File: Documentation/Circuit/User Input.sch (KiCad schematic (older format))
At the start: 1 part

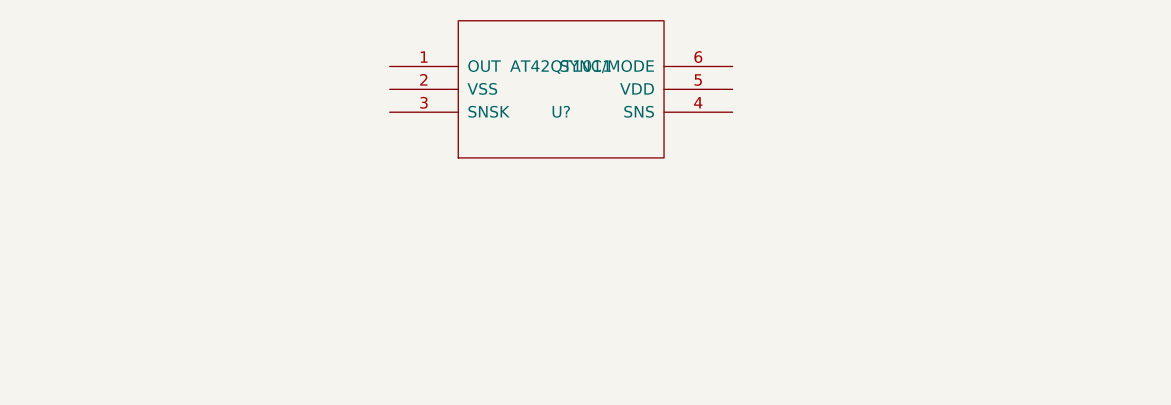
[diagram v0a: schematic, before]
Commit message: Worked on schematic and PCB
Worked on circuit schematic.  Circuits utilized should reflect those in
the BLE112 and AT42 datasheets.  Added initial PCB layout.  Routing
still needs to be done for PCB layout.  Circuit layout should be double
checked before routing.  Refer to an-kd02_103 for more details on touch
interface layout.  Refer to tps62732 datasheet for more details on power
system layout.
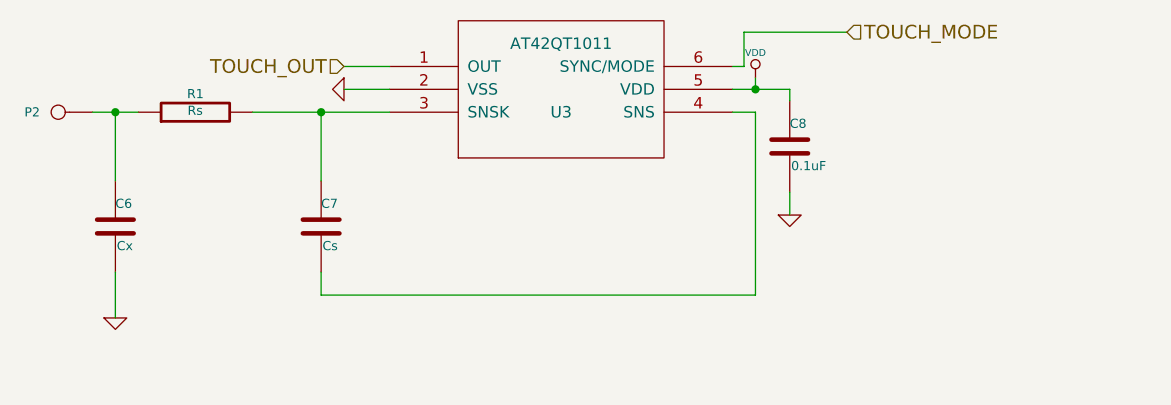
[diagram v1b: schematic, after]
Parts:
- added C6: Cx, ~, symbol C
- added C7: Cs, ~, symbol C
- added C8: 0.1uF, ~, symbol C
- added P2: CONN_1, symbol CONN_1
- added R1: Rs, ~, symbol R
- gave numbers to parts that had none: 1
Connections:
- net TOUCH_OUT: now reaches U3.1 (OUT)
- net GND: now reaches U3.2 (VSS)
- net GND: now also C6.2, C8.2
- net at U3.3 (SNSK): now also C7.1, R1.2
- net at U3.4 (SNS): now also C7.2
- net VDD: now reaches U3.5 (VDD)
- net VDD: now also C8.1
- net TOUCH_MODE: now reaches U3.6 (SYNC/MODE)
- new net: C6.1, P2.1, R1.1
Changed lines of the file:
@@
 Sheet 3 3
 Title ""
-Date "2 jun 2015"
+Date "4 jun 2015"
 Rev ""
 Comp ""
@@
 $EndDescr
 $Comp
-L AT42QT1011 U?
+L AT42QT1011 U3
 U 1 1 556D309E
 P 5450 3600
-F 0 "U?" H 5450 3500 50  0000 C CNN
-F 1 "AT42QT1011" H 5450 3700 50  0000 C CNN
+F 0 "U3" H 5450 3500 50  0000 C CNN
+F 1 "AT42QT1011" H 5450 3800 50  0000 C CNN
 F 2 "MODULE" H 5450 3600 50  0001 C CNN
 F 3 "DOCUMENTATION" H 5450 3600 50  0001 C CNN
@@
 	1    0    0    -1
 $EndComp
+$Comp
+L R R1
+U 1 1 556F5E65
+P 3850 3700
+F 0 "R1" V 3930 3700 40  0000 C CNN
+F 1 "Rs" V 3857 3701 40  0000 C CNN
+F 2 "~" V 3780 3700 30  0000 C CNN
+F 3 "~" H 3850 3700 30  0000 C CNN
+	1    3850 3700
+	0    -1   -1   0
+$EndComp
+$Comp
+L C C7
+U 1 1 556F5E74
+P 4400 4200
+F 0 "C7" H 4400 4300 40  0000 L CNN
+F 1 "Cs" H 4406 4115 40  0000 L CNN
+F 2 "~" H 4438 4050 30  0000 C CNN
+F 3 "~" H 4400 4200 60  0000 C CNN
+	1    4400 4200
+	1    0    0    -1
+$EndComp
+$Comp
+L GND #PWR22
+U 1 1 556F5E91
+P 4500 3600
+F 0 "#PWR22" H 4500 3600 30  0001 C CNN
+F 1 "GND" H 4500 3530 30  0001 C CNN
+F 2 "" H 4500 3600 60  0000 C CNN
+F 3 "" H 4500 3600 60  0000 C CNN
+	1    4500 3600
+	0    1    1    0
+$EndComp
+Wire Wire Line
+	4700 3600 4500 3600
+Wire Wire Line
+	4700 3700 4100 3700
+Wire Wire Line
+	4400 3700 4400 4000
+Connection ~ 4400 3700
+Wire Wire Line
+	4400 4400 4400 4500
+Wire Wire Line
+	6300 3700 6300 4500
+Wire Wire Line
+	6300 3700 6200 3700
+Wire Wire Line
+	6300 4500 4400 4500
+Text HLabel 4500 3500 0    60   Input ~ 0
+TOUCH_OUT
+Wire Wire Line
+	4700 3500 4500 3500
+$Comp
+L VDD #PWR23
+U 1 1 556F5F2B
+P 6300 3550
+F 0 "#PWR23" H 6300 3650 30  0001 C CNN
+F 1 "VDD" H 6300 3660 30  0000 C CNN
+F 2 "" H 6300 3550 60  0000 C CNN
+F 3 "" H 6300 3550 60  0000 C CNN
+	1    6300 3550
+	1    0    0    -1
+$EndComp
+Wire Wire Line
+	6200 3600 6450 3600
+Wire Wire Line
+	6300 3600 6300 3550
+$Comp
+L CONN_1 P2
+U 1 1 556F60DB
+P 3250 3700
+F 0 "P2" H 3330 3700 40  0000 L CNN
+F 1 "CONN_1" H 3250 3755 30  0001 C CNN
+F 2 "" H 3250 3700 60  0000 C CNN
+F 3 "" H 3250 3700 60  0000 C CNN
+	1    3250 3700
+	-1   0    0    1
+$EndComp
+Wire Wire Line
+	3600 3700 3400 3700
+Wire Wire Line
+	3500 3700 3500 4000
+Connection ~ 3500 3700
+$Comp
+L C C6
+U 1 1 556F6108
+P 3500 4200
+F 0 "C6" H 3500 4300 40  0000 L CNN
+F 1 "Cx" H 3506 4115 40  0000 L CNN
+F 2 "~" H 3538 4050 30  0000 C CNN
+F 3 "~" H 3500 4200 60  0000 C CNN
+	1    3500 4200
+	1    0    0    -1
+$EndComp
+$Comp
+L GND #PWR21
+U 1 1 556F6117
+P 3500 4600
+F 0 "#PWR21" H 3500 4600 30  0001 C CNN
+F 1 "GND" H 3500 4530 30  0001 C CNN
+F 2 "" H 3500 4600 60  0000 C CNN
+F 3 "" H 3500 4600 60  0000 C CNN
+	1    3500 4600
+	1    0    0    -1
+$EndComp
+Wire Wire Line
+	3500 4400 3500 4600
+Wire Wire Line
+	6200 3500 6250 3500
+Wire Wire Line
+	6250 3500 6250 3350
+Wire Wire Line
+	6250 3350 6700 3350
+Text HLabel 6700 3350 2    60   Input ~ 0
+TOUCH_MODE
+$Comp
+L C C8
+U 1 1 556F65DC
+P 6450 3850
+F 0 "C8" H 6450 3950 40  0000 L CNN
+F 1 "0.1uF" H 6456 3765 40  0000 L CNN
+F 2 "~" H 6488 3700 30  0000 C CNN
+F 3 "~" H 6450 3850 60  0000 C CNN
+	1    6450 3850
+	1    0    0    -1
+$EndComp
+Wire Wire Line
+	6450 3600 6450 3650
+Connection ~ 6300 3600
+$Comp
+L GND #PWR24
+U 1 1 556F65FE
+P 6450 4150
+F 0 "#PWR24" H 6450 4150 30  0001 C CNN
+F 1 "GND" H 6450 4080 30  0001 C CNN
+F 2 "" H 6450 4150 60  0000 C CNN
+F 3 "" H 6450 4150 60  0000 C CNN
+	1    6450 4150
+	1    0    0    -1
+$EndComp
+Wire Wire Line
+	6450 4050 6450 4150
 $EndSCHEMATC

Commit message: Modified input circuitry, remade PCB
Changed input circuit from Atmel's QTouch chipset to a simple momentary
pushbutton, added datasheet for said pushbutton.  Button is dust tight
and waterproof as per spec doc.

Changed passives to use 0603 footprint instead of 0402 to provide easier
reflowing.

Performed initial layout, connectivity, and ground pours.

Still pending are circuit connectivity and feasibility, and PCB
connectivity checks.  Parts might be purchased at this point.  Parts
will then be compared against footprints to ensure fit before sending
gerbers (and order) off to PCB fab.
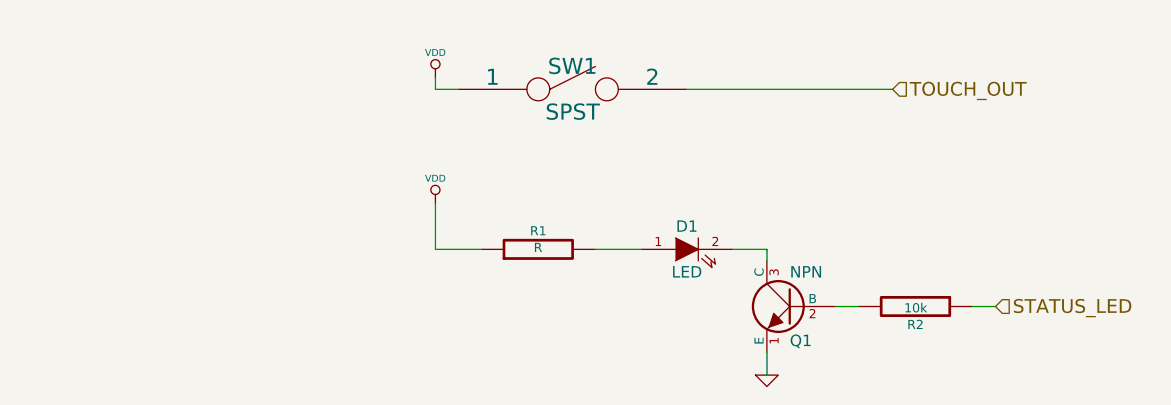
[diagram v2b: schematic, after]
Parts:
- removed C6: Cx, ~, symbol C
- removed C7: Cs, ~, symbol C
- removed C8: 0.1uF, ~, symbol C
- removed P2: CONN_1, symbol CONN_1
- removed U3: AT42QT1011, MODULE, symbol AT42QT1011
- added D1: LED, ~, symbol LED
- added Q1: NPN, ~, symbol NPN
- added R2: 10k, ~, symbol R
- added SW1: SPST, ~, symbol SPST
- R1: value Rs -> R
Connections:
- net GND: now also Q1.1 (E)
- net TOUCH_OUT: now also SW1.2
- net VDD: now also R1.1, SW1.1
- net at R1.2: now also D1.1 (A)
- new net: Q1.2 (B), R2.2
- new net: D1.2 (K), Q1.3 (C)
- new net STATUS_LED: R2.1
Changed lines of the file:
@@
 Sheet 3 3
 Title ""
-Date "4 jun 2015"
+Date "7 jun 2015"
 Rev ""
 Comp ""
@@
 $EndDescr
 $Comp
-L AT42QT1011 U3
-U 1 1 556D309E
-P 5450 3600
-F 0 "U3" H 5450 3500 50  0000 C CNN
-F 1 "AT42QT1011" H 5450 3800 50  0000 C CNN
-F 2 "MODULE" H 5450 3600 50  0001 C CNN
-F 3 "DOCUMENTATION" H 5450 3600 50  0001 C CNN
-	1    5450 3600
+L SPST SW1
+U 1 1 55736C53
+P 5500 3600
+F 0 "SW1" H 5500 3700 70  0000 C CNN
+F 1 "SPST" H 5500 3500 70  0000 C CNN
+F 2 "~" H 5500 3600 60  0000 C CNN
+F 3 "~" H 5500 3600 60  0000 C CNN
+	1    5500 3600
+	1    0    0    -1
+$EndComp
+$Comp
+L VDD #PWR022
+U 1 1 55736C71
+P 4900 3550
+F 0 "#PWR022" H 4900 3650 30  0001 C CNN
+F 1 "VDD" H 4900 3660 30  0000 C CNN
+F 2 "" H 4900 3550 60  0000 C CNN
+F 3 "" H 4900 3550 60  0000 C CNN
+	1    4900 3550
+	1    0    0    -1
+$EndComp
+Wire Wire Line
+	5000 3600 4900 3600
+Wire Wire Line
+	4900 3600 4900 3550
+Wire Wire Line
+	6000 3600 6900 3600
+Text HLabel 6900 3600 2    60   Input ~ 0
+TOUCH_OUT
+$Comp
+L VDD #PWR023
+U 1 1 5573998C
+P 4900 4100
+F 0 "#PWR023" H 4900 4200 30  0001 C CNN
+F 1 "VDD" H 4900 4210 30  0000 C CNN
+F 2 "" H 4900 4100 60  0000 C CNN
+F 3 "" H 4900 4100 60  0000 C CNN
+	1    4900 4100
+	1    0    0    -1
+$EndComp
+$Comp
+L NPN Q1
+U 1 1 5573999B
+P 6450 4550
+F 0 "Q1" H 6450 4400 50  0000 R CNN
+F 1 "NPN" H 6450 4700 50  0000 R CNN
+F 2 "~" H 6450 4550 60  0000 C CNN
+F 3 "~" H 6450 4550 60  0000 C CNN
+	1    6450 4550
+	-1   0    0    -1
+$EndComp
+$Comp
+L LED D1
+U 1 1 55739A1C
+P 6000 4300
+F 0 "D1" H 6000 4400 50  0000 C CNN
+F 1 "LED" H 6000 4200 50  0000 C CNN
+F 2 "~" H 6000 4300 60  0000 C CNN
+F 3 "~" H 6000 4300 60  0000 C CNN
+	1    6000 4300
 	1    0    0    -1
 $EndComp
 $Comp
 L R R1
-U 1 1 556F5E65
-P 3850 3700
-F 0 "R1" V 3930 3700 40  0000 C CNN
-F 1 "Rs" V 3857 3701 40  0000 C CNN
-F 2 "~" V 3780 3700 30  0000 C CNN
-F 3 "~" H 3850 3700 30  0000 C CNN
-	1    3850 3700
+U 1 1 55739A49
+P 5350 4300
+F 0 "R1" V 5430 4300 40  0000 C CNN
+F 1 "R" V 5357 4301 40  0000 C CNN
+F 2 "~" V 5280 4300 30  0000 C CNN
+F 3 "~" H 5350 4300 30  0000 C CNN
+	1    5350 4300
 	0    -1   -1   0
 $EndComp
+Wire Wire Line
+	4900 4300 5100 4300
+Wire Wire Line
+	5600 4300 5800 4300
 $Comp
-L C C7
-U 1 1 556F5E74
-P 4400 4200
-F 0 "C7" H 4400 4300 40  0000 L CNN
-F 1 "Cs" H 4406 4115 40  0000 L CNN
-F 2 "~" H 4438 4050 30  0000 C CNN
-F 3 "~" H 4400 4200 60  0000 C CNN
-	1    4400 4200
+L GND #PWR024
+U 1 1 55739AEF
+P 6350 4850
+F 0 "#PWR024" H 6350 4850 30  0001 C CNN
+F 1 "GND" H 6350 4780 30  0001 C CNN
+F 2 "" H 6350 4850 60  0000 C CNN
+F 3 "" H 6350 4850 60  0000 C CNN
+	1    6350 4850
 	1    0    0    -1
 $EndComp
+Wire Wire Line
+	6350 4750 6350 4850
+Wire Wire Line
+	6200 4300 6350 4300
+Wire Wire Line
+	6350 4300 6350 4350
+Wire Wire Line
+	4900 4100 4900 4300
+Text HLabel 7350 4550 2    60   Input ~ 0
+STATUS_LED
 $Comp
-L GND #PWR22
-U 1 1 556F5E91
-P 4500 3600
-F 0 "#PWR22" H 4500 3600 30  0001 C CNN
-F 1 "GND" H 4500 3530 30  0001 C CNN
-F 2 "" H 4500 3600 60  0000 C CNN
-F 3 "" H 4500 3600 60  0000 C CNN
-	1    4500 3600
+L R R2
+U 1 1 5573AA89
+P 7000 4550
+F 0 "R2" V 7080 4550 40  0000 C CNN
+F 1 "10k" V 7007 4551 40  0000 C CNN
+F 2 "~" V 6930 4550 30  0000 C CNN
+F 3 "~" H 7000 4550 30  0000 C CNN
+	1    7000 4550
 	0    1    1    0
 $EndComp
 Wire Wire Line
-	4700 3600 4500 3600
+	6650 4550 6750 4550
 Wire Wire Line
-	4700 3700 4100 3700
-Wire Wire Line
-	4400 3700 4400 4000
-Connection ~ 4400 3700
-Wire Wire Line
-	4400 4400 4400 4500
-Wire Wire Line
-	6300 3700 6300 4500
-Wire Wire Line
-	6300 3700 6200 3700
-Wire Wire Line
-	6300 4500 4400 4500
-Text HLabel 4500 3500 0    60   Input ~ 0
-TOUCH_OUT
-Wire Wire Line
-	4700 3500 4500 3500
-$Comp
-L VDD #PWR23
-U 1 1 556F5F2B
-P 6300 3550
-F 0 "#PWR23" H 6300 3650 30  0001 C CNN
-F 1 "VDD" H 6300 3660 30  0000 C CNN
-F 2 "" H 6300 3550 60  0000 C CNN
-F 3 "" H 6300 3550 60  0000 C CNN
-	1    6300 3550
-	1    0    0    -1
-$EndComp
-Wire Wire Line
-	6200 3600 6450 3600
-Wire Wire Line
-	6300 3600 6300 3550
-$Comp
-L CONN_1 P2
-U 1 1 556F60DB
-P 3250 3700
-F 0 "P2" H 3330 3700 40  0000 L CNN
-F 1 "CONN_1" H 3250 3755 30  0001 C CNN
-F 2 "" H 3250 3700 60  0000 C CNN
-F 3 "" H 3250 3700 60  0000 C CNN
-	1    3250 3700
-	-1   0    0    1
-$EndComp
-Wire Wire Line
-	3600 3700 3400 3700
-Wire Wire Line
-	3500 3700 3500 4000
-Connection ~ 3500 3700
-$Comp
-L C C6
-U 1 1 556F6108
-P 3500 4200
-F 0 "C6" H 3500 4300 40  0000 L CNN
-F 1 "Cx" H 3506 4115 40  0000 L CNN
-F 2 "~" H 3538 4050 30  0000 C CNN
-F 3 "~" H 3500 4200 60  0000 C CNN
-	1    3500 4200
-	1    0    0    -1
-$EndComp
-$Comp
-L GND #PWR21
-U 1 1 556F6117
-P 3500 4600
-F 0 "#PWR21" H 3500 4600 30  0001 C CNN
-F 1 "GND" H 3500 4530 30  0001 C CNN
-F 2 "" H 3500 4600 60  0000 C CNN
-F 3 "" H 3500 4600 60  0000 C CNN
-	1    3500 4600
-	1    0    0    -1
-$EndComp
-Wire Wire Line
-	3500 4400 3500 4600
-Wire Wire Line
-	6200 3500 6250 3500
-Wire Wire Line
-	6250 3500 6250 3350
-Wire Wire Line
-	6250 3350 6700 3350
-Text HLabel 6700 3350 2    60   Input ~ 0
-TOUCH_MODE
-$Comp
-L C C8
-U 1 1 556F65DC
-P 6450 3850
-F 0 "C8" H 6450 3950 40  0000 L CNN
-F 1 "0.1uF" H 6456 3765 40  0000 L CNN
-F 2 "~" H 6488 3700 30  0000 C CNN
-F 3 "~" H 6450 3850 60  0000 C CNN
-	1    6450 3850
-	1    0    0    -1
-$EndComp
-Wire Wire Line
-	6450 3600 6450 3650
-Connection ~ 6300 3600
-$Comp
-L GND #PWR24
-U 1 1 556F65FE
-P 6450 4150
-F 0 "#PWR24" H 6450 4150 30  0001 C CNN
-F 1 "GND" H 6450 4080 30  0001 C CNN
-F 2 "" H 6450 4150 60  0000 C CNN
-F 3 "" H 6450 4150 60  0000 C CNN
-	1    6450 4150
-	1    0    0    -1
-$EndComp
-Wire Wire Line
-	6450 4050 6450 4150
+	7250 4550 7350 4550
 $EndSCHEMATC

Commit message: Added BoM, OSHpark estimate
Added BoM, added estimated cost for board fabrication from OSHpark.
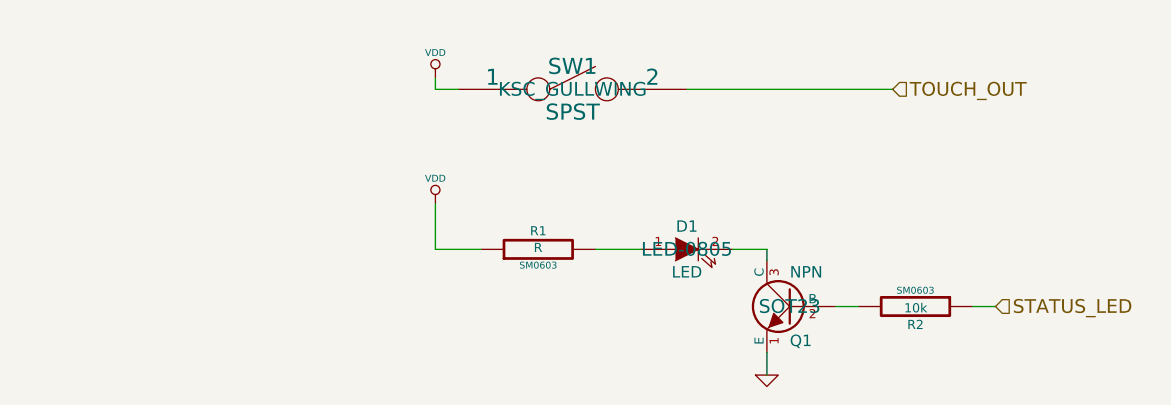
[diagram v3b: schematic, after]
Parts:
- D1: footprint ~ -> LED-0805
- Q1: footprint ~ -> SOT23
- R1, R2: footprint ~ -> SM0603
- SW1: footprint ~ -> KSC_GULLWING
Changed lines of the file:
@@
 Sheet 3 3
 Title ""
-Date "7 jun 2015"
+Date "11 jun 2015"
 Rev ""
 Comp ""
@@
 F 0 "SW1" H 5500 3700 70  0000 C CNN
 F 1 "SPST" H 5500 3500 70  0000 C CNN
-F 2 "~" H 5500 3600 60  0000 C CNN
+F 2 "KSC_GULLWING" H 5500 3600 60  0000 C CNN
 F 3 "~" H 5500 3600 60  0000 C CNN
 	1    5500 3600
@@
 F 0 "Q1" H 6450 4400 50  0000 R CNN
 F 1 "NPN" H 6450 4700 50  0000 R CNN
-F 2 "~" H 6450 4550 60  0000 C CNN
+F 2 "SOT23" H 6450 4550 60  0000 C CNN
 F 3 "~" H 6450 4550 60  0000 C CNN
 	1    6450 4550
@@
 F 0 "D1" H 6000 4400 50  0000 C CNN
 F 1 "LED" H 6000 4200 50  0000 C CNN
-F 2 "~" H 6000 4300 60  0000 C CNN
+F 2 "LED-0805" H 6000 4300 60  0000 C CNN
 F 3 "~" H 6000 4300 60  0000 C CNN
 	1    6000 4300
@@
 F 0 "R1" V 5430 4300 40  0000 C CNN
 F 1 "R" V 5357 4301 40  0000 C CNN
-F 2 "~" V 5280 4300 30  0000 C CNN
+F 2 "SM0603" V 5280 4300 30  0000 C CNN
 F 3 "~" H 5350 4300 30  0000 C CNN
 	1    5350 4300
@@
 F 0 "R2" V 7080 4550 40  0000 C CNN
 F 1 "10k" V 7007 4551 40  0000 C CNN
-F 2 "~" V 6930 4550 30  0000 C CNN
+F 2 "SM0603" V 6930 4550 30  0000 C CNN
 F 3 "~" H 7000 4550 30  0000 C CNN
 	1    7000 4550
